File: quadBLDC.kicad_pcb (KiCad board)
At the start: 2 copper layers, 100 x 100 mm, 167 parts, among them IC1 STM32G474RET6, J1 CAN_CONN, J10 VOUT_C, J11 VOUT_D, J2 RS422_CONN, J3 SPI, J4 SWD, J5 Encoder, J6 VDC, J7 GND, J8 VOUT_A, J9 VOUT_B, Q1 NTMFS5C670NL, Q2 NTMFS5C670NL, Q3 NTMFS5C670NL, Q4 NTMFS5C670NL, Q5 NTMFS5C670NL, Q6 NTMFS5C670NL, Q7 NTMFS5C670NL, Q8 NTMFS5C670NL, SW1 RST, SW2 SW_DIP_x04, U1 LM5109BMA, U10 NJU77701F, U11 MCP1825S, U12 MP2456GJ-Z, U13 TLV75533PDBV, U14 TLV75533PDBV, U15 MCP2562-E-SN, U16 ST1480ABDR, U17 AM26LV32ACPWR, U18 SI8621AB-B-ISR, U2 NJU77701F, U3 NJU77701F, U4 LM5109BMA, U5 NJU77701F, U6 LM5109BMA, U7 NJU77701F, U8 NJU77701F, U9 LM5109BMA, Y1 Resonator_Small

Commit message: wip
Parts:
- moved C10 53.4 mm to (81.5, 38.0)
- moved C9 53.4 mm to (76.5, 35.0)
- moved R10 53.4 mm to (80.5, 31.5)
- moved R11 53.4 mm to (84.5, 35.0)
- moved R13 53.4 mm to (78.5, 35.0)
- moved R9 53.4 mm to (82.5, 31.5)
- moved U3 53.4 mm to (81.5, 35.0)
- moved C31 13.3 mm to (88.0, 30.5), turned to 180 degrees
- moved C34 13.2 mm to (88.0, 41.0)
- moved C36 13.2 mm to (88.0, 43.5)
- moved C41 13.2 mm to (88.0, 49.5)
- moved U11 13.2 mm to (91.0, 35.5)
- moved U13 13.2 mm to (88.0, 46.5)
- moved C37 13.2 mm to (93.0, 43.5)
- moved C40 13.2 mm to (93.0, 49.5)
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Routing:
- net GND: track 41.9 -> 39.4 mm
- net Net-(R40-Pad2): track 3.53 -> 2.13 mm
- net VDC: track 8.48 -> 7.81 mm

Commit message: wip
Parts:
- C44, C45, C47, C48, C49, C50, C51, C52, C53: moved to B.Cu
- moved R46 108.5 mm to (81.0, 92.0), turned to 270 degrees
- moved U17 107.7 mm to (82.5, 85.5), turned to 90 degrees
- moved R47 98.5 mm to (83.0, 92.0), turned to 270 degrees
- moved R48 98.2 mm to (85.0, 92.0), turned to 270 degrees
- moved U16 87.1 mm to (65.5, 87.5), turned to 270 degrees
- moved C45 78.0 mm to (65.5, 90.0), turned to 180 degrees
- moved R49 76.4 mm to (65.5, 92.5)
- moved R45 74.2 mm to (52.0, 92.5), turned to 180 degrees
- moved C47 72.8 mm to (45.0, 90.0), turned to 180 degrees
- moved C48 69.4 mm to (45.0, 85.0)
- moved U15 66.5 mm to (52.0, 87.5), turned to 270 degrees
- moved C44 56.2 mm to (52.0, 85.0)
- moved U18 53.8 mm to (45.0, 87.5), turned to 270 degrees
- moved J3 52.5 mm to (25.0, 96.5)
- moved C46 44.9 mm to (78.5, 85.5), turned to 270 degrees
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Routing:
- net GND: track 39.4 -> 195.3 mm, vias 62 -> 116
- net GNDA: track 0.00 -> 139.1 mm, vias 0 -> 10
- net +3.3VA: track 0.00 -> 119.9 mm, vias 0 -> 9
- net /MCU/ENC_A: track 0.00 -> 73.4 mm, vias 0 -> 4
- net /SPI_NSS: track 0.00 -> 71.7 mm, vias 0 -> 2
- net /MCU/ENC_B: track 0.00 -> 70.7 mm, vias 0 -> 4
- net /Inverter/GATE_DL: track 0.00 -> 68.4 mm, vias 0 -> 4
- net /SPI_SCK: track 0.00 -> 62.3 mm, vias 0 -> 2
- net /Inverter/GATE_DH: track 0.00 -> 58.2 mm, vias 0 -> 2
- net /SPI_MISO: track 0.00 -> 57.8 mm, vias 0 -> 2
- net /MCU/ENC_Z: track 0.00 -> 55.3 mm, vias 0 -> 2
- net /Inverter/SENSE_ID: track 0.00 -> 55.1 mm, vias 0 -> 2
- net /SPI_MOSI: track 0.00 -> 55.1 mm, vias 0 -> 2
- net /MCU/CAN_RD: track 0.00 -> 54.1 mm, vias 0 -> 2
- net VCOM: track 0.00 -> 51.9 mm, vias 0 -> 5
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
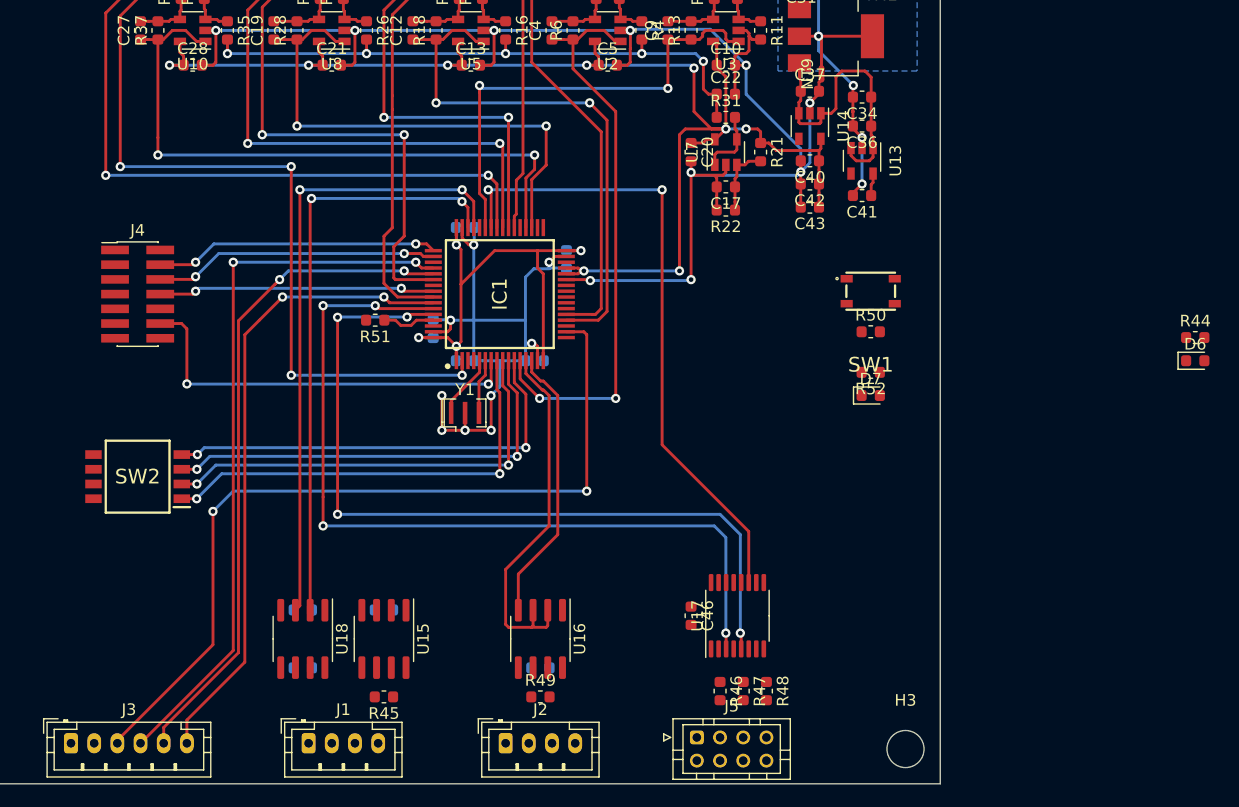
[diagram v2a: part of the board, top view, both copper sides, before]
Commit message: wip CAN STBYピン修正
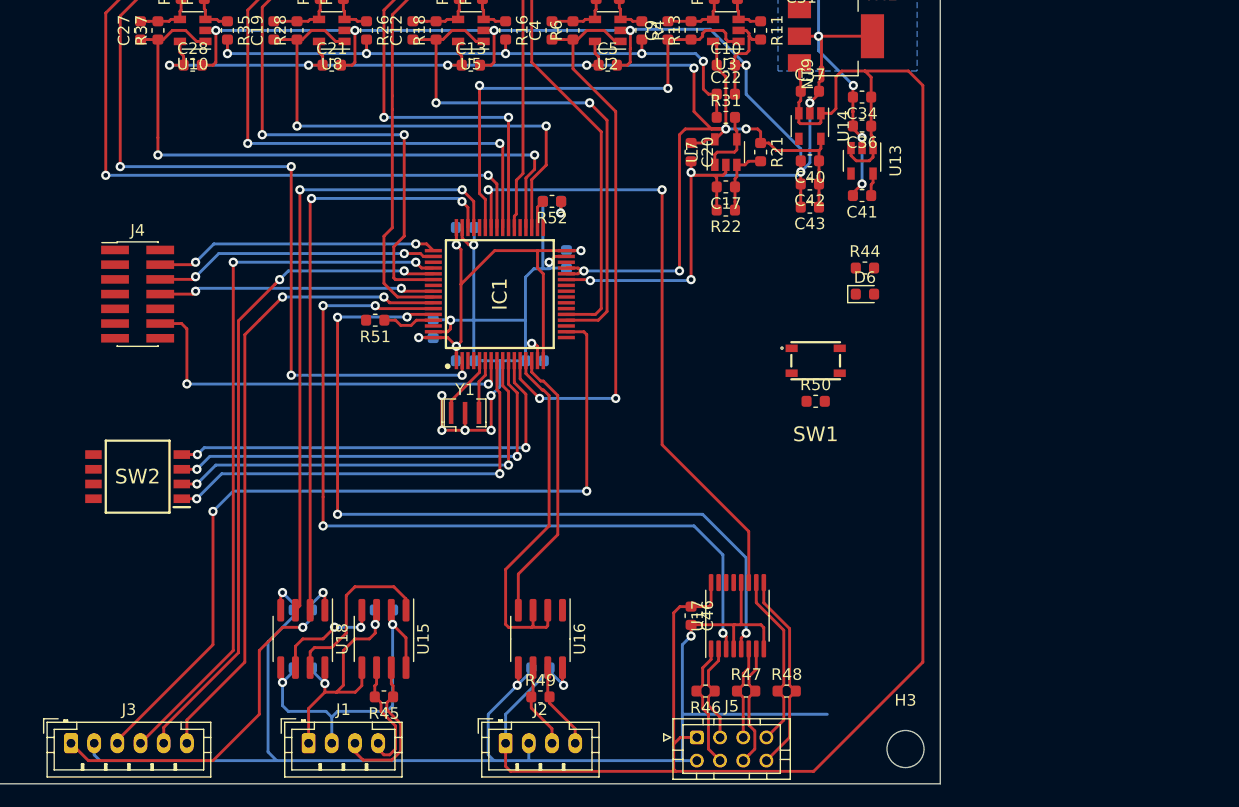
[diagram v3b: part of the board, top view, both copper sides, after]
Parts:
- D7: moved to B.Cu
- moved D7 32.2 mm to (66.5, 49.8)
- moved R52 31.2 mm to (66.5, 49.8)
- moved R44 29.1 mm to (93.5, 55.5)
- moved D6 29.1 mm to (93.5, 57.8)
- moved R50 7.65 mm to (89.2, 67.0)
- moved SW1 7.65 mm to (89.2, 63.5)
- moved R48 1.75 mm to (86.8, 92.0), turned to 0 degrees
- moved R46 1.25 mm to (79.8, 92.0), turned to 180 degrees
- moved R47 0.25 mm to (83.2, 92.0), turned to 0 degrees
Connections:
- U15 pad 8: +5VD -> GNDD
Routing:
- net +5V: track 25.5 -> 155.9 mm, vias 0 -> 1
- net GND: track 195.3 -> 323.4 mm, vias 116 -> 119
- net +3V3: track 43.8 -> 77.8 mm, vias 4 -> 6
- net GNDD: track 0.00 -> 31.3 mm, vias 0 -> 2
- net +5VD: track 0.00 -> 24.4 mm, vias 0 -> 2
- net /ENC_Z-: track 0.00 -> 17.5 mm
- net /ENC_Z+: track 0.00 -> 15.4 mm
- net Net-(U15-Pad1): track 0.00 -> 15.3 mm
- net /CAN_H: track 0.00 -> 13.3 mm
- net /ENC_A-: track 0.00 -> 11.0 mm
- net /ENC_B-: track 0.00 -> 11.0 mm
- net /CAN_L: track 0.00 -> 10.3 mm
- net Net-(U15-Pad4): track 0.00 -> 9.69 mm, vias 0 -> 2
- net /ENC_A+: track 0.00 -> 8.83 mm
- net /ENC_B+: track 0.00 -> 8.28 mm
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
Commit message: Update : 配線一段落
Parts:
- added REF**: Pin_D1.0mm_L10.0mm, Connector_Pin:Pin_D1.0mm_L10.0mm, B.Cu at (5.08, 12.7)
- added REF**: Pin_D1.0mm_L10.0mm, Connector_Pin:Pin_D1.0mm_L10.0mm, B.Cu at (17.8, 83.8)
- added REF**: Pin_D1.0mm_L10.0mm, Connector_Pin:Pin_D1.0mm_L10.0mm, B.Cu at (15.2, 73.7)
- added REF**: Pin_D1.0mm_L10.0mm, Connector_Pin:Pin_D1.0mm_L10.0mm, B.Cu at (12.7, 66.0)
- added REF**: Pin_D1.0mm_L10.0mm, Connector_Pin:Pin_D1.0mm_L10.0mm, B.Cu at (17.8, 71.1)
- added REF**: Pin_D1.0mm_L10.0mm, Connector_Pin:Pin_D1.0mm_L10.0mm, B.Cu at (10.2, 68.6)
- added REF**: Pin_D1.0mm_L10.0mm, Connector_Pin:Pin_D1.0mm_L10.0mm, B.Cu at (15.2, 68.6)
- added REF**: Pin_D1.0mm_L10.0mm, Connector_Pin:Pin_D1.0mm_L10.0mm, B.Cu at (5.08, 73.7)
- added REF**: Pin_D1.0mm_L10.0mm, Connector_Pin:Pin_D1.0mm_L10.0mm, B.Cu at (10.2, 73.7)
- added REF**: Pin_D1.0mm_L10.0mm, Connector_Pin:Pin_D1.0mm_L10.0mm, B.Cu at (2.54, 66.0)
- added REF**: Pin_D1.0mm_L10.0mm, Connector_Pin:Pin_D1.0mm_L10.0mm, B.Cu at (5.08, 66.0)
- added REF**: Pin_D1.0mm_L10.0mm, Connector_Pin:Pin_D1.0mm_L10.0mm, B.Cu at (12.7, 73.7)
- added REF**: Pin_D1.0mm_L10.0mm, Connector_Pin:Pin_D1.0mm_L10.0mm, B.Cu at (2.54, 83.8)
- added REF**: Pin_D1.0mm_L10.0mm, Connector_Pin:Pin_D1.0mm_L10.0mm, B.Cu at (5.08, 71.1)
- added REF**: Pin_D1.0mm_L10.0mm, Connector_Pin:Pin_D1.0mm_L10.0mm, B.Cu at (20.3, 66.0)
- added REF**: Pin_D1.0mm_L10.0mm, Connector_Pin:Pin_D1.0mm_L10.0mm, B.Cu at (17.8, 68.6)
- added REF**: Pin_D1.0mm_L10.0mm, Connector_Pin:Pin_D1.0mm_L10.0mm, B.Cu at (20.3, 63.5)
- added REF**: Pin_D1.0mm_L10.0mm, Connector_Pin:Pin_D1.0mm_L10.0mm, B.Cu at (15.2, 61.0)
- added REF**: Pin_D1.0mm_L10.0mm, Connector_Pin:Pin_D1.0mm_L10.0mm, B.Cu at (20.3, 61.0)
- added REF**: Pin_D1.0mm_L10.0mm, Connector_Pin:Pin_D1.0mm_L10.0mm, B.Cu at (12.7, 61.0)
- added REF**: Pin_D1.0mm_L10.0mm, Connector_Pin:Pin_D1.0mm_L10.0mm, B.Cu at (17.8, 73.7)
- added REF**: Pin_D1.0mm_L10.0mm, Connector_Pin:Pin_D1.0mm_L10.0mm, B.Cu at (15.2, 66.0)
- added REF**: Pin_D1.0mm_L10.0mm, Connector_Pin:Pin_D1.0mm_L10.0mm, B.Cu at (10.2, 61.0)
- added REF**: Pin_D1.0mm_L10.0mm, Connector_Pin:Pin_D1.0mm_L10.0mm, B.Cu at (15.2, 81.3)
- added REF**: Pin_D1.0mm_L10.0mm, Connector_Pin:Pin_D1.0mm_L10.0mm, B.Cu at (5.08, 55.9)
- added REF**: Pin_D1.0mm_L10.0mm, Connector_Pin:Pin_D1.0mm_L10.0mm, B.Cu at (20.3, 68.6)
- added REF**: Pin_D1.0mm_L10.0mm, Connector_Pin:Pin_D1.0mm_L10.0mm, B.Cu at (10.2, 55.9)
- added REF**: Pin_D1.0mm_L10.0mm, Connector_Pin:Pin_D1.0mm_L10.0mm, B.Cu at (10.2, 63.5)
- added REF**: Pin_D1.0mm_L10.0mm, Connector_Pin:Pin_D1.0mm_L10.0mm, B.Cu at (7.62, 68.6)
- added REF**: Pin_D1.0mm_L10.0mm, Connector_Pin:Pin_D1.0mm_L10.0mm, B.Cu at (2.54, 61.0)
- added REF**: Pin_D1.0mm_L10.0mm, Connector_Pin:Pin_D1.0mm_L10.0mm, B.Cu at (2.54, 58.4)
- added REF**: Pin_D1.0mm_L10.0mm, Connector_Pin:Pin_D1.0mm_L10.0mm, B.Cu at (15.2, 58.4)
- added REF**: Pin_D1.0mm_L10.0mm, Connector_Pin:Pin_D1.0mm_L10.0mm, B.Cu at (7.62, 58.4)
- added REF**: Pin_D1.0mm_L10.0mm, Connector_Pin:Pin_D1.0mm_L10.0mm, B.Cu at (12.7, 58.4)
- added REF**: Pin_D1.0mm_L10.0mm, Connector_Pin:Pin_D1.0mm_L10.0mm, B.Cu at (20.3, 83.8)
- added REF**: Pin_D1.0mm_L10.0mm, Connector_Pin:Pin_D1.0mm_L10.0mm, B.Cu at (15.2, 55.9)
- added REF**: Pin_D1.0mm_L10.0mm, Connector_Pin:Pin_D1.0mm_L10.0mm, B.Cu at (7.62, 63.5)
- added REF**: Pin_D1.0mm_L10.0mm, Connector_Pin:Pin_D1.0mm_L10.0mm, B.Cu at (17.8, 61.0)
- added REF**: Pin_D1.0mm_L10.0mm, Connector_Pin:Pin_D1.0mm_L10.0mm, B.Cu at (5.08, 61.0)
- added REF**: Pin_D1.0mm_L10.0mm, Connector_Pin:Pin_D1.0mm_L10.0mm, B.Cu at (15.2, 63.5)
- added REF**: Pin_D1.0mm_L10.0mm, Connector_Pin:Pin_D1.0mm_L10.0mm, B.Cu at (10.2, 58.4)
- added REF**: Pin_D1.0mm_L10.0mm, Connector_Pin:Pin_D1.0mm_L10.0mm, B.Cu at (17.8, 63.5)
- added REF**: Pin_D1.0mm_L10.0mm, Connector_Pin:Pin_D1.0mm_L10.0mm, B.Cu at (12.7, 55.9)
- added REF**: Pin_D1.0mm_L10.0mm, Connector_Pin:Pin_D1.0mm_L10.0mm, B.Cu at (5.08, 58.4)
- added REF**: Pin_D1.0mm_L10.0mm, Connector_Pin:Pin_D1.0mm_L10.0mm, B.Cu at (7.62, 61.0)
- added REF**: Pin_D1.0mm_L10.0mm, Connector_Pin:Pin_D1.0mm_L10.0mm, B.Cu at (15.2, 83.8)
- added REF**: Pin_D1.0mm_L10.0mm, Connector_Pin:Pin_D1.0mm_L10.0mm, B.Cu at (12.7, 63.5)
- added REF**: Pin_D1.0mm_L10.0mm, Connector_Pin:Pin_D1.0mm_L10.0mm, B.Cu at (20.3, 58.4)
- added REF**: Pin_D1.0mm_L10.0mm, Connector_Pin:Pin_D1.0mm_L10.0mm, B.Cu at (17.8, 55.9)
- added REF**: Pin_D1.0mm_L10.0mm, Connector_Pin:Pin_D1.0mm_L10.0mm, B.Cu at (20.3, 55.9)
- added REF**: Pin_D1.0mm_L10.0mm, Connector_Pin:Pin_D1.0mm_L10.0mm, B.Cu at (2.54, 55.9)
- added REF**: Pin_D1.0mm_L10.0mm, Connector_Pin:Pin_D1.0mm_L10.0mm, B.Cu at (7.62, 55.9)
- added REF**: Pin_D1.0mm_L10.0mm, Connector_Pin:Pin_D1.0mm_L10.0mm, B.Cu at (5.08, 63.5)
- added REF**: Pin_D1.0mm_L10.0mm, Connector_Pin:Pin_D1.0mm_L10.0mm, B.Cu at (15.2, 50.8)
- added REF**: Pin_D1.0mm_L10.0mm, Connector_Pin:Pin_D1.0mm_L10.0mm, B.Cu at (10.2, 50.8)
- added REF**: Pin_D1.0mm_L10.0mm, Connector_Pin:Pin_D1.0mm_L10.0mm, B.Cu at (10.2, 53.3)
- added REF**: Pin_D1.0mm_L10.0mm, Connector_Pin:Pin_D1.0mm_L10.0mm, B.Cu at (7.62, 83.8)
- added REF**: Pin_D1.0mm_L10.0mm, Connector_Pin:Pin_D1.0mm_L10.0mm, B.Cu at (12.7, 50.8)
- added REF**: Pin_D1.0mm_L10.0mm, Connector_Pin:Pin_D1.0mm_L10.0mm, B.Cu at (2.54, 48.3)
- added REF**: Pin_D1.0mm_L10.0mm, Connector_Pin:Pin_D1.0mm_L10.0mm, B.Cu at (17.8, 50.8)
- added REF**: Pin_D1.0mm_L10.0mm, Connector_Pin:Pin_D1.0mm_L10.0mm, B.Cu at (10.2, 45.7)
- added REF**: Pin_D1.0mm_L10.0mm, Connector_Pin:Pin_D1.0mm_L10.0mm, B.Cu at (5.08, 53.3)
- added REF**: Pin_D1.0mm_L10.0mm, Connector_Pin:Pin_D1.0mm_L10.0mm, B.Cu at (15.2, 53.3)
- added REF**: Pin_D1.0mm_L10.0mm, Connector_Pin:Pin_D1.0mm_L10.0mm, B.Cu at (20.3, 50.8)
- added REF**: Pin_D1.0mm_L10.0mm, Connector_Pin:Pin_D1.0mm_L10.0mm, B.Cu at (7.62, 45.7)
- added REF**: Pin_D1.0mm_L10.0mm, Connector_Pin:Pin_D1.0mm_L10.0mm, B.Cu at (2.54, 53.3)
- added REF**: Pin_D1.0mm_L10.0mm, Connector_Pin:Pin_D1.0mm_L10.0mm, B.Cu at (12.7, 53.3)
- added REF**: Pin_D1.0mm_L10.0mm, Connector_Pin:Pin_D1.0mm_L10.0mm, B.Cu at (17.8, 81.3)
- added REF**: Pin_D1.0mm_L10.0mm, Connector_Pin:Pin_D1.0mm_L10.0mm, B.Cu at (5.08, 50.8)
- added REF**: Pin_D1.0mm_L10.0mm, Connector_Pin:Pin_D1.0mm_L10.0mm, B.Cu at (17.8, 53.3)
- added REF**: Pin_D1.0mm_L10.0mm, Connector_Pin:Pin_D1.0mm_L10.0mm, B.Cu at (20.3, 48.3)
- added REF**: Pin_D1.0mm_L10.0mm, Connector_Pin:Pin_D1.0mm_L10.0mm, B.Cu at (15.2, 45.7)
- added REF**: Pin_D1.0mm_L10.0mm, Connector_Pin:Pin_D1.0mm_L10.0mm, B.Cu at (20.3, 53.3)
- added REF**: Pin_D1.0mm_L10.0mm, Connector_Pin:Pin_D1.0mm_L10.0mm, B.Cu at (12.7, 45.7)
- added REF**: Pin_D1.0mm_L10.0mm, Connector_Pin:Pin_D1.0mm_L10.0mm, B.Cu at (7.62, 50.8)
- added REF**: Pin_D1.0mm_L10.0mm, Connector_Pin:Pin_D1.0mm_L10.0mm, B.Cu at (2.54, 50.8)
- added REF**: Pin_D1.0mm_L10.0mm, Connector_Pin:Pin_D1.0mm_L10.0mm, B.Cu at (7.62, 53.3)
- added REF**: Pin_D1.0mm_L10.0mm, Connector_Pin:Pin_D1.0mm_L10.0mm, B.Cu at (5.08, 20.3)
- added REF**: Pin_D1.0mm_L10.0mm, Connector_Pin:Pin_D1.0mm_L10.0mm, B.Cu at (5.08, 83.8)
- added REF**: Pin_D1.0mm_L10.0mm, Connector_Pin:Pin_D1.0mm_L10.0mm, B.Cu at (5.08, 15.2)
- added REF**: Pin_D1.0mm_L10.0mm, Connector_Pin:Pin_D1.0mm_L10.0mm, B.Cu at (12.7, 15.2)
- added REF**: Pin_D1.0mm_L10.0mm, Connector_Pin:Pin_D1.0mm_L10.0mm, B.Cu at (12.7, 17.8)
- added REF**: Pin_D1.0mm_L10.0mm, Connector_Pin:Pin_D1.0mm_L10.0mm, B.Cu at (17.8, 22.9)
- added REF**: Pin_D1.0mm_L10.0mm, Connector_Pin:Pin_D1.0mm_L10.0mm, B.Cu at (2.54, 15.2)
- added REF**: Pin_D1.0mm_L10.0mm, Connector_Pin:Pin_D1.0mm_L10.0mm, B.Cu at (2.54, 20.3)
- added REF**: Pin_D1.0mm_L10.0mm, Connector_Pin:Pin_D1.0mm_L10.0mm, B.Cu at (15.2, 22.9)
- added REF**: Pin_D1.0mm_L10.0mm, Connector_Pin:Pin_D1.0mm_L10.0mm, B.Cu at (12.7, 22.9)
- added REF**: Pin_D1.0mm_L10.0mm, Connector_Pin:Pin_D1.0mm_L10.0mm, B.Cu at (5.08, 22.9)
- added REF**: Pin_D1.0mm_L10.0mm, Connector_Pin:Pin_D1.0mm_L10.0mm, B.Cu at (20.3, 15.2)
- added REF**: Pin_D1.0mm_L10.0mm, Connector_Pin:Pin_D1.0mm_L10.0mm, B.Cu at (2.54, 86.4)
- added REF**: Pin_D1.0mm_L10.0mm, Connector_Pin:Pin_D1.0mm_L10.0mm, B.Cu at (7.62, 17.8)
- added REF**: Pin_D1.0mm_L10.0mm, Connector_Pin:Pin_D1.0mm_L10.0mm, B.Cu at (10.2, 22.9)
- added REF**: Pin_D1.0mm_L10.0mm, Connector_Pin:Pin_D1.0mm_L10.0mm, B.Cu at (10.2, 15.2)
- added REF**: Pin_D1.0mm_L10.0mm, Connector_Pin:Pin_D1.0mm_L10.0mm, B.Cu at (15.2, 17.8)
- added REF**: Pin_D1.0mm_L10.0mm, Connector_Pin:Pin_D1.0mm_L10.0mm, B.Cu at (2.54, 17.8)
- added REF**: Pin_D1.0mm_L10.0mm, Connector_Pin:Pin_D1.0mm_L10.0mm, B.Cu at (20.3, 17.8)
- added REF**: Pin_D1.0mm_L10.0mm, Connector_Pin:Pin_D1.0mm_L10.0mm, B.Cu at (15.2, 15.2)
- added REF**: Pin_D1.0mm_L10.0mm, Connector_Pin:Pin_D1.0mm_L10.0mm, B.Cu at (10.2, 17.8)
- added REF**: Pin_D1.0mm_L10.0mm, Connector_Pin:Pin_D1.0mm_L10.0mm, B.Cu at (17.8, 20.3)
- added REF**: Pin_D1.0mm_L10.0mm, Connector_Pin:Pin_D1.0mm_L10.0mm, B.Cu at (17.8, 17.8)
- added REF**: Pin_D1.0mm_L10.0mm, Connector_Pin:Pin_D1.0mm_L10.0mm, B.Cu at (7.62, 86.4)
- added REF**: Pin_D1.0mm_L10.0mm, Connector_Pin:Pin_D1.0mm_L10.0mm, B.Cu at (10.2, 38.1)
- added REF**: Pin_D1.0mm_L10.0mm, Connector_Pin:Pin_D1.0mm_L10.0mm, B.Cu at (2.54, 38.1)
- added REF**: Pin_D1.0mm_L10.0mm, Connector_Pin:Pin_D1.0mm_L10.0mm, B.Cu at (5.08, 33.0)
- added REF**: Pin_D1.0mm_L10.0mm, Connector_Pin:Pin_D1.0mm_L10.0mm, B.Cu at (15.2, 38.1)
- added REF**: Pin_D1.0mm_L10.0mm, Connector_Pin:Pin_D1.0mm_L10.0mm, B.Cu at (2.54, 33.0)
- added REF**: Pin_D1.0mm_L10.0mm, Connector_Pin:Pin_D1.0mm_L10.0mm, B.Cu at (20.3, 33.0)
- added REF**: Pin_D1.0mm_L10.0mm, Connector_Pin:Pin_D1.0mm_L10.0mm, B.Cu at (17.8, 30.5)
- added REF**: Pin_D1.0mm_L10.0mm, Connector_Pin:Pin_D1.0mm_L10.0mm, B.Cu at (15.2, 35.6)
- added REF**: Pin_D1.0mm_L10.0mm, Connector_Pin:Pin_D1.0mm_L10.0mm, B.Cu at (10.2, 30.5)
- added REF**: Pin_D1.0mm_L10.0mm, Connector_Pin:Pin_D1.0mm_L10.0mm, B.Cu at (20.3, 35.6)
- added REF**: Pin_D1.0mm_L10.0mm, Connector_Pin:Pin_D1.0mm_L10.0mm, B.Cu at (15.2, 86.4)
- added REF**: Pin_D1.0mm_L10.0mm, Connector_Pin:Pin_D1.0mm_L10.0mm, B.Cu at (10.2, 83.8)
- added REF**: Pin_D1.0mm_L10.0mm, Connector_Pin:Pin_D1.0mm_L10.0mm, B.Cu at (5.08, 30.5)
- added REF**: Pin_D1.0mm_L10.0mm, Connector_Pin:Pin_D1.0mm_L10.0mm, B.Cu at (20.3, 38.1)
- added REF**: Pin_D1.0mm_L10.0mm, Connector_Pin:Pin_D1.0mm_L10.0mm, B.Cu at (10.2, 35.6)
- added REF**: Pin_D1.0mm_L10.0mm, Connector_Pin:Pin_D1.0mm_L10.0mm, B.Cu at (12.7, 35.6)
- added REF**: Pin_D1.0mm_L10.0mm, Connector_Pin:Pin_D1.0mm_L10.0mm, B.Cu at (17.8, 33.0)
- added REF**: Pin_D1.0mm_L10.0mm, Connector_Pin:Pin_D1.0mm_L10.0mm, B.Cu at (7.62, 38.1)
- added REF**: Pin_D1.0mm_L10.0mm, Connector_Pin:Pin_D1.0mm_L10.0mm, B.Cu at (12.7, 38.1)
- added REF**: Pin_D1.0mm_L10.0mm, Connector_Pin:Pin_D1.0mm_L10.0mm, B.Cu at (15.2, 30.5)
- added REF**: Pin_D1.0mm_L10.0mm, Connector_Pin:Pin_D1.0mm_L10.0mm, B.Cu at (15.2, 33.0)
- added REF**: Pin_D1.0mm_L10.0mm, Connector_Pin:Pin_D1.0mm_L10.0mm, B.Cu at (7.62, 33.0)
- added REF**: Pin_D1.0mm_L10.0mm, Connector_Pin:Pin_D1.0mm_L10.0mm, B.Cu at (20.3, 81.3)
- added REF**: Pin_D1.0mm_L10.0mm, Connector_Pin:Pin_D1.0mm_L10.0mm, B.Cu at (2.54, 35.6)
- added REF**: Pin_D1.0mm_L10.0mm, Connector_Pin:Pin_D1.0mm_L10.0mm, B.Cu at (7.62, 35.6)
- added REF**: Pin_D1.0mm_L10.0mm, Connector_Pin:Pin_D1.0mm_L10.0mm, B.Cu at (10.2, 33.0)
- added REF**: Pin_D1.0mm_L10.0mm, Connector_Pin:Pin_D1.0mm_L10.0mm, B.Cu at (20.3, 30.5)
- added REF**: Pin_D1.0mm_L10.0mm, Connector_Pin:Pin_D1.0mm_L10.0mm, B.Cu at (12.7, 33.0)
- added REF**: Pin_D1.0mm_L10.0mm, Connector_Pin:Pin_D1.0mm_L10.0mm, B.Cu at (2.54, 30.5)
- added REF**: Pin_D1.0mm_L10.0mm, Connector_Pin:Pin_D1.0mm_L10.0mm, B.Cu at (17.8, 35.6)
- added REF**: Pin_D1.0mm_L10.0mm, Connector_Pin:Pin_D1.0mm_L10.0mm, B.Cu at (5.08, 35.6)
- added REF**: Pin_D1.0mm_L10.0mm, Connector_Pin:Pin_D1.0mm_L10.0mm, B.Cu at (12.7, 30.5)
- added REF**: Pin_D1.0mm_L10.0mm, Connector_Pin:Pin_D1.0mm_L10.0mm, B.Cu at (15.2, 25.4)
- added REF**: Pin_D1.0mm_L10.0mm, Connector_Pin:Pin_D1.0mm_L10.0mm, B.Cu at (12.7, 83.8)
- added REF**: Pin_D1.0mm_L10.0mm, Connector_Pin:Pin_D1.0mm_L10.0mm, B.Cu at (10.2, 25.4)
- added REF**: Pin_D1.0mm_L10.0mm, Connector_Pin:Pin_D1.0mm_L10.0mm, B.Cu at (5.08, 38.1)
- added REF**: Pin_D1.0mm_L10.0mm, Connector_Pin:Pin_D1.0mm_L10.0mm, B.Cu at (10.2, 27.9)
- added REF**: Pin_D1.0mm_L10.0mm, Connector_Pin:Pin_D1.0mm_L10.0mm, B.Cu at (20.3, 25.4)
- added REF**: Pin_D1.0mm_L10.0mm, Connector_Pin:Pin_D1.0mm_L10.0mm, B.Cu at (7.62, 27.9)
- added REF**: Pin_D1.0mm_L10.0mm, Connector_Pin:Pin_D1.0mm_L10.0mm, B.Cu at (7.62, 30.5)
- added REF**: Pin_D1.0mm_L10.0mm, Connector_Pin:Pin_D1.0mm_L10.0mm, B.Cu at (12.7, 27.9)
- added REF**: Pin_D1.0mm_L10.0mm, Connector_Pin:Pin_D1.0mm_L10.0mm, B.Cu at (15.2, 27.9)
- added REF**: Pin_D1.0mm_L10.0mm, Connector_Pin:Pin_D1.0mm_L10.0mm, B.Cu at (20.3, 27.9)
- added REF**: Pin_D1.0mm_L10.0mm, Connector_Pin:Pin_D1.0mm_L10.0mm, B.Cu at (17.8, 38.1)
- added REF**: Pin_D1.0mm_L10.0mm, Connector_Pin:Pin_D1.0mm_L10.0mm, B.Cu at (2.54, 81.3)
- added REF**: Pin_D1.0mm_L10.0mm, Connector_Pin:Pin_D1.0mm_L10.0mm, B.Cu at (12.7, 25.4)
- added REF**: Pin_D1.0mm_L10.0mm, Connector_Pin:Pin_D1.0mm_L10.0mm, B.Cu at (5.08, 27.9)
- added REF**: Pin_D1.0mm_L10.0mm, Connector_Pin:Pin_D1.0mm_L10.0mm, B.Cu at (2.54, 22.9)
- added REF**: Pin_D1.0mm_L10.0mm, Connector_Pin:Pin_D1.0mm_L10.0mm, B.Cu at (17.8, 25.4)
- added REF**: Pin_D1.0mm_L10.0mm, Connector_Pin:Pin_D1.0mm_L10.0mm, B.Cu at (10.2, 20.3)
- added REF**: Pin_D1.0mm_L10.0mm, Connector_Pin:Pin_D1.0mm_L10.0mm, B.Cu at (7.62, 20.3)
- added REF**: Pin_D1.0mm_L10.0mm, Connector_Pin:Pin_D1.0mm_L10.0mm, B.Cu at (7.62, 15.2)
- added REF**: Pin_D1.0mm_L10.0mm, Connector_Pin:Pin_D1.0mm_L10.0mm, B.Cu at (5.08, 17.8)
- added REF**: Pin_D1.0mm_L10.0mm, Connector_Pin:Pin_D1.0mm_L10.0mm, B.Cu at (15.2, 20.3)
- added REF**: Pin_D1.0mm_L10.0mm, Connector_Pin:Pin_D1.0mm_L10.0mm, B.Cu at (17.8, 15.2)
- added REF**: Pin_D1.0mm_L10.0mm, Connector_Pin:Pin_D1.0mm_L10.0mm, B.Cu at (7.62, 81.3)
- added REF**: Pin_D1.0mm_L10.0mm, Connector_Pin:Pin_D1.0mm_L10.0mm, B.Cu at (12.7, 20.3)
- added REF**: Pin_D1.0mm_L10.0mm, Connector_Pin:Pin_D1.0mm_L10.0mm, B.Cu at (20.3, 22.9)
- added REF**: Pin_D1.0mm_L10.0mm, Connector_Pin:Pin_D1.0mm_L10.0mm, B.Cu at (2.54, 27.9)
- added REF**: Pin_D1.0mm_L10.0mm, Connector_Pin:Pin_D1.0mm_L10.0mm, B.Cu at (7.62, 22.9)
- added REF**: Pin_D1.0mm_L10.0mm, Connector_Pin:Pin_D1.0mm_L10.0mm, B.Cu at (20.3, 20.3)
- added REF**: Pin_D1.0mm_L10.0mm, Connector_Pin:Pin_D1.0mm_L10.0mm, B.Cu at (2.54, 25.4)
- added REF**: Pin_D1.0mm_L10.0mm, Connector_Pin:Pin_D1.0mm_L10.0mm, B.Cu at (5.08, 25.4)
- added REF**: Pin_D1.0mm_L10.0mm, Connector_Pin:Pin_D1.0mm_L10.0mm, B.Cu at (7.62, 25.4)
- added REF**: Pin_D1.0mm_L10.0mm, Connector_Pin:Pin_D1.0mm_L10.0mm, B.Cu at (17.8, 27.9)
- added REF**: Pin_D1.0mm_L10.0mm, Connector_Pin:Pin_D1.0mm_L10.0mm, B.Cu at (20.3, 88.9)
- added REF**: Pin_D1.0mm_L10.0mm, Connector_Pin:Pin_D1.0mm_L10.0mm, B.Cu at (17.8, 86.4)
- added REF**: Pin_D1.0mm_L10.0mm, Connector_Pin:Pin_D1.0mm_L10.0mm, B.Cu at (10.2, 88.9)
- added REF**: Pin_D1.0mm_L10.0mm, Connector_Pin:Pin_D1.0mm_L10.0mm, B.Cu at (7.62, 88.9)
- added REF**: Pin_D1.0mm_L10.0mm, Connector_Pin:Pin_D1.0mm_L10.0mm, B.Cu at (12.7, 88.9)
- added REF**: Pin_D1.0mm_L10.0mm, Connector_Pin:Pin_D1.0mm_L10.0mm, B.Cu at (15.2, 88.9)
- added REF**: Pin_D1.0mm_L10.0mm, Connector_Pin:Pin_D1.0mm_L10.0mm, B.Cu at (17.8, 88.9)
- added REF**: Pin_D1.0mm_L10.0mm, Connector_Pin:Pin_D1.0mm_L10.0mm, B.Cu at (5.08, 88.9)
- added REF**: Pin_D1.0mm_L10.0mm, Connector_Pin:Pin_D1.0mm_L10.0mm, B.Cu at (2.54, 88.9)
- added REF**: Pin_D1.0mm_L10.0mm, Connector_Pin:Pin_D1.0mm_L10.0mm, B.Cu at (5.08, 86.4)
- added REF**: Pin_D1.0mm_L10.0mm, Connector_Pin:Pin_D1.0mm_L10.0mm, B.Cu at (12.7, 81.3)
- added REF**: Pin_D1.0mm_L10.0mm, Connector_Pin:Pin_D1.0mm_L10.0mm, B.Cu at (12.7, 12.7)
- added REF**: Pin_D1.0mm_L10.0mm, Connector_Pin:Pin_D1.0mm_L10.0mm, B.Cu at (2.54, 12.7)
- added REF**: Pin_D1.0mm_L10.0mm, Connector_Pin:Pin_D1.0mm_L10.0mm, B.Cu at (20.3, 12.7)
- added REF**: Pin_D1.0mm_L10.0mm, Connector_Pin:Pin_D1.0mm_L10.0mm, B.Cu at (10.2, 12.7)
- added REF**: Pin_D1.0mm_L10.0mm, Connector_Pin:Pin_D1.0mm_L10.0mm, B.Cu at (17.8, 12.7)
- added REF**: Pin_D1.0mm_L10.0mm, Connector_Pin:Pin_D1.0mm_L10.0mm, B.Cu at (20.3, 10.2)
- added REF**: Pin_D1.0mm_L10.0mm, Connector_Pin:Pin_D1.0mm_L10.0mm, B.Cu at (7.62, 10.2)
- added REF**: Pin_D1.0mm_L10.0mm, Connector_Pin:Pin_D1.0mm_L10.0mm, B.Cu at (15.2, 10.2)
- added REF**: Pin_D1.0mm_L10.0mm, Connector_Pin:Pin_D1.0mm_L10.0mm, B.Cu at (7.62, 12.7)
- added REF**: Pin_D1.0mm_L10.0mm, Connector_Pin:Pin_D1.0mm_L10.0mm, B.Cu at (12.7, 10.2)
- added REF**: Pin_D1.0mm_L10.0mm, Connector_Pin:Pin_D1.0mm_L10.0mm, B.Cu at (5.08, 10.2)
- added REF**: Pin_D1.0mm_L10.0mm, Connector_Pin:Pin_D1.0mm_L10.0mm, B.Cu at (17.8, 10.2)
- added REF**: Pin_D1.0mm_L10.0mm, Connector_Pin:Pin_D1.0mm_L10.0mm, B.Cu at (2.54, 10.2)
- added REF**: Pin_D1.0mm_L10.0mm, Connector_Pin:Pin_D1.0mm_L10.0mm, B.Cu at (15.2, 12.7)
- added REF**: Pin_D1.0mm_L10.0mm, Connector_Pin:Pin_D1.0mm_L10.0mm, B.Cu at (10.2, 10.2)
- added REF**: Pin_D1.0mm_L10.0mm, Connector_Pin:Pin_D1.0mm_L10.0mm, B.Cu at (2.54, 40.6)
- added REF**: Pin_D1.0mm_L10.0mm, Connector_Pin:Pin_D1.0mm_L10.0mm, B.Cu at (12.7, 43.2)
- added REF**: Pin_D1.0mm_L10.0mm, Connector_Pin:Pin_D1.0mm_L10.0mm, B.Cu at (5.08, 45.7)
- added REF**: Pin_D1.0mm_L10.0mm, Connector_Pin:Pin_D1.0mm_L10.0mm, B.Cu at (7.62, 48.3)
- added REF**: Pin_D1.0mm_L10.0mm, Connector_Pin:Pin_D1.0mm_L10.0mm, B.Cu at (5.08, 43.2)
- added REF**: Pin_D1.0mm_L10.0mm, Connector_Pin:Pin_D1.0mm_L10.0mm, B.Cu at (10.2, 48.3)
- added REF**: Pin_D1.0mm_L10.0mm, Connector_Pin:Pin_D1.0mm_L10.0mm, B.Cu at (5.08, 40.6)
- added REF**: Pin_D1.0mm_L10.0mm, Connector_Pin:Pin_D1.0mm_L10.0mm, B.Cu at (12.7, 40.6)
- added REF**: Pin_D1.0mm_L10.0mm, Connector_Pin:Pin_D1.0mm_L10.0mm, B.Cu at (5.08, 48.3)
- added REF**: Pin_D1.0mm_L10.0mm, Connector_Pin:Pin_D1.0mm_L10.0mm, B.Cu at (10.2, 86.4)
- added REF**: Pin_D1.0mm_L10.0mm, Connector_Pin:Pin_D1.0mm_L10.0mm, B.Cu at (17.8, 43.2)
- added REF**: Pin_D1.0mm_L10.0mm, Connector_Pin:Pin_D1.0mm_L10.0mm, B.Cu at (17.8, 48.3)
- added REF**: Pin_D1.0mm_L10.0mm, Connector_Pin:Pin_D1.0mm_L10.0mm, B.Cu at (2.54, 45.7)
- added REF**: Pin_D1.0mm_L10.0mm, Connector_Pin:Pin_D1.0mm_L10.0mm, B.Cu at (20.3, 43.2)
- added REF**: Pin_D1.0mm_L10.0mm, Connector_Pin:Pin_D1.0mm_L10.0mm, B.Cu at (17.8, 45.7)
- added REF**: Pin_D1.0mm_L10.0mm, Connector_Pin:Pin_D1.0mm_L10.0mm, B.Cu at (10.2, 43.2)
- added REF**: Pin_D1.0mm_L10.0mm, Connector_Pin:Pin_D1.0mm_L10.0mm, B.Cu at (7.62, 43.2)
- added REF**: Pin_D1.0mm_L10.0mm, Connector_Pin:Pin_D1.0mm_L10.0mm, B.Cu at (15.2, 48.3)
- added REF**: Pin_D1.0mm_L10.0mm, Connector_Pin:Pin_D1.0mm_L10.0mm, B.Cu at (20.3, 40.6)
- added REF**: Pin_D1.0mm_L10.0mm, Connector_Pin:Pin_D1.0mm_L10.0mm, B.Cu at (20.3, 45.7)
- added REF**: Pin_D1.0mm_L10.0mm, Connector_Pin:Pin_D1.0mm_L10.0mm, B.Cu at (10.2, 81.3)
- added REF**: Pin_D1.0mm_L10.0mm, Connector_Pin:Pin_D1.0mm_L10.0mm, B.Cu at (10.2, 40.6)
- added REF**: Pin_D1.0mm_L10.0mm, Connector_Pin:Pin_D1.0mm_L10.0mm, B.Cu at (7.62, 40.6)
- added REF**: Pin_D1.0mm_L10.0mm, Connector_Pin:Pin_D1.0mm_L10.0mm, B.Cu at (2.54, 43.2)
- added REF**: Pin_D1.0mm_L10.0mm, Connector_Pin:Pin_D1.0mm_L10.0mm, B.Cu at (17.8, 40.6)
- added REF**: Pin_D1.0mm_L10.0mm, Connector_Pin:Pin_D1.0mm_L10.0mm, B.Cu at (15.2, 40.6)
- added REF**: Pin_D1.0mm_L10.0mm, Connector_Pin:Pin_D1.0mm_L10.0mm, B.Cu at (15.2, 43.2)
- added REF**: Pin_D1.0mm_L10.0mm, Connector_Pin:Pin_D1.0mm_L10.0mm, B.Cu at (12.7, 48.3)
- added REF**: Pin_D1.0mm_L10.0mm, Connector_Pin:Pin_D1.0mm_L10.0mm, B.Cu at (15.2, 76.2)
- added REF**: Pin_D1.0mm_L10.0mm, Connector_Pin:Pin_D1.0mm_L10.0mm, B.Cu at (10.2, 76.2)
- added REF**: Pin_D1.0mm_L10.0mm, Connector_Pin:Pin_D1.0mm_L10.0mm, B.Cu at (10.2, 78.7)
- added REF**: Pin_D1.0mm_L10.0mm, Connector_Pin:Pin_D1.0mm_L10.0mm, B.Cu at (20.3, 86.4)
- added REF**: Pin_D1.0mm_L10.0mm, Connector_Pin:Pin_D1.0mm_L10.0mm, B.Cu at (12.7, 76.2)
- added REF**: Pin_D1.0mm_L10.0mm, Connector_Pin:Pin_D1.0mm_L10.0mm, B.Cu at (20.3, 76.2)
- added REF**: Pin_D1.0mm_L10.0mm, Connector_Pin:Pin_D1.0mm_L10.0mm, B.Cu at (20.3, 78.7)
- added REF**: Pin_D1.0mm_L10.0mm, Connector_Pin:Pin_D1.0mm_L10.0mm, B.Cu at (7.62, 78.7)
- added REF**: Pin_D1.0mm_L10.0mm, Connector_Pin:Pin_D1.0mm_L10.0mm, B.Cu at (12.7, 78.7)
- added REF**: Pin_D1.0mm_L10.0mm, Connector_Pin:Pin_D1.0mm_L10.0mm, B.Cu at (15.2, 78.7)
- added REF**: Pin_D1.0mm_L10.0mm, Connector_Pin:Pin_D1.0mm_L10.0mm, B.Cu at (7.62, 76.2)
- added REF**: Pin_D1.0mm_L10.0mm, Connector_Pin:Pin_D1.0mm_L10.0mm, B.Cu at (2.54, 78.7)
- added REF**: Pin_D1.0mm_L10.0mm, Connector_Pin:Pin_D1.0mm_L10.0mm, B.Cu at (2.54, 76.2)
- added REF**: Pin_D1.0mm_L10.0mm, Connector_Pin:Pin_D1.0mm_L10.0mm, B.Cu at (17.8, 76.2)
- added REF**: Pin_D1.0mm_L10.0mm, Connector_Pin:Pin_D1.0mm_L10.0mm, B.Cu at (5.08, 81.3)
- added REF**: Pin_D1.0mm_L10.0mm, Connector_Pin:Pin_D1.0mm_L10.0mm, B.Cu at (5.08, 76.2)
- added REF**: Pin_D1.0mm_L10.0mm, Connector_Pin:Pin_D1.0mm_L10.0mm, B.Cu at (17.8, 78.7)
- added REF**: Pin_D1.0mm_L10.0mm, Connector_Pin:Pin_D1.0mm_L10.0mm, B.Cu at (5.08, 78.7)
- added REF**: Pin_D1.0mm_L10.0mm, Connector_Pin:Pin_D1.0mm_L10.0mm, B.Cu at (2.54, 73.7)
- added REF**: Pin_D1.0mm_L10.0mm, Connector_Pin:Pin_D1.0mm_L10.0mm, B.Cu at (20.3, 73.7)
- added REF**: Pin_D1.0mm_L10.0mm, Connector_Pin:Pin_D1.0mm_L10.0mm, B.Cu at (15.2, 71.1)
- added REF**: Pin_D1.0mm_L10.0mm, Connector_Pin:Pin_D1.0mm_L10.0mm, B.Cu at (10.2, 71.1)
- added REF**: Pin_D1.0mm_L10.0mm, Connector_Pin:Pin_D1.0mm_L10.0mm, B.Cu at (12.7, 71.1)
- added REF**: Pin_D1.0mm_L10.0mm, Connector_Pin:Pin_D1.0mm_L10.0mm, B.Cu at (7.62, 71.1)
- added REF**: Pin_D1.0mm_L10.0mm, Connector_Pin:Pin_D1.0mm_L10.0mm, B.Cu at (17.8, 58.4)
- added REF**: Pin_D1.0mm_L10.0mm, Connector_Pin:Pin_D1.0mm_L10.0mm, B.Cu at (12.7, 86.4)
- added REF**: Pin_D1.0mm_L10.0mm, Connector_Pin:Pin_D1.0mm_L10.0mm, B.Cu at (7.62, 66.0)
- added REF**: Pin_D1.0mm_L10.0mm, Connector_Pin:Pin_D1.0mm_L10.0mm, B.Cu at (17.8, 66.0)
- added REF**: Pin_D1.0mm_L10.0mm, Connector_Pin:Pin_D1.0mm_L10.0mm, B.Cu at (5.08, 68.6)
- added REF**: Pin_D1.0mm_L10.0mm, Connector_Pin:Pin_D1.0mm_L10.0mm, B.Cu at (7.62, 73.7)
- added REF**: Pin_D1.0mm_L10.0mm, Connector_Pin:Pin_D1.0mm_L10.0mm, B.Cu at (2.54, 63.5)
- added REF**: Pin_D1.0mm_L10.0mm, Connector_Pin:Pin_D1.0mm_L10.0mm, B.Cu at (20.3, 71.1)
- added REF**: Pin_D1.0mm_L10.0mm, Connector_Pin:Pin_D1.0mm_L10.0mm, B.Cu at (10.2, 66.0)
- added REF**: Pin_D1.0mm_L10.0mm, Connector_Pin:Pin_D1.0mm_L10.0mm, B.Cu at (12.7, 68.6)
- added REF**: Pin_D1.0mm_L10.0mm, Connector_Pin:Pin_D1.0mm_L10.0mm, B.Cu at (2.54, 68.6)
- added REF**: Pin_D1.0mm_L10.0mm, Connector_Pin:Pin_D1.0mm_L10.0mm, B.Cu at (2.54, 71.1)
- moved R50 5.00 mm to (93.2, 70.0)
- moved SW1 5.00 mm to (93.2, 66.5)
- moved D6 2.02 mm to (93.2, 59.8)
- moved R44 2.02 mm to (93.2, 57.5)
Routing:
- net +3V3: track 77.8 -> 232.4 mm, vias 6 -> 12
- net /T_VCP_RX: track 0.00 -> 64.9 mm, vias 0 -> 4
- net /T_VCP_TX: track 0.00 -> 63.7 mm, vias 0 -> 4
- net +12V: track 34.9 -> 96.4 mm, vias 4 -> 5
- net /T_NRST: track 35.4 -> 72.4 mm, vias 2 -> 5
- net /MCU/RS485_RO: track 0.00 -> 31.5 mm
- net VDC: track 26.7 -> 42.7 mm
- net GND: track 323.4 -> 313.6 mm, vias 119 -> 126
- net /Inverter/GATE_DL: track 68.4 -> 60.5 mm, vias 4 -> 0
- net /SPI_NSS: track 71.7 -> 65.2 mm
- net /Inverter/GATE_DH: track 58.2 -> 52.1 mm
- net /Inverter/GATE_CH: track 46.7 -> 41.6 mm
- net /Inverter/SENSE_ID: track 55.1 -> 51.4 mm
- net /Inverter/GATE_CL: track 45.3 -> 41.5 mm
- net /Inverter/SENSE_IA: track 49.6 -> 46.6 mm
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- added copper zone on B.Cu, net GNDA
